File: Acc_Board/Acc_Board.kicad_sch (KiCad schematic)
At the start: 43 parts, among them J1 1053091202, J11 1053091202, J12 776087-1, J2 1053091202, J3 1053091202, J4 1053091202, J5 1053091202, J6 1053091202, J9 1053091202, K1 Relay_SPST-NO, U1 ISO1050DUB, U13 R-78B5.0-2.0, U2 NUCLEO-L432KC, U4 PQDE6W-Q110-S5-H-D

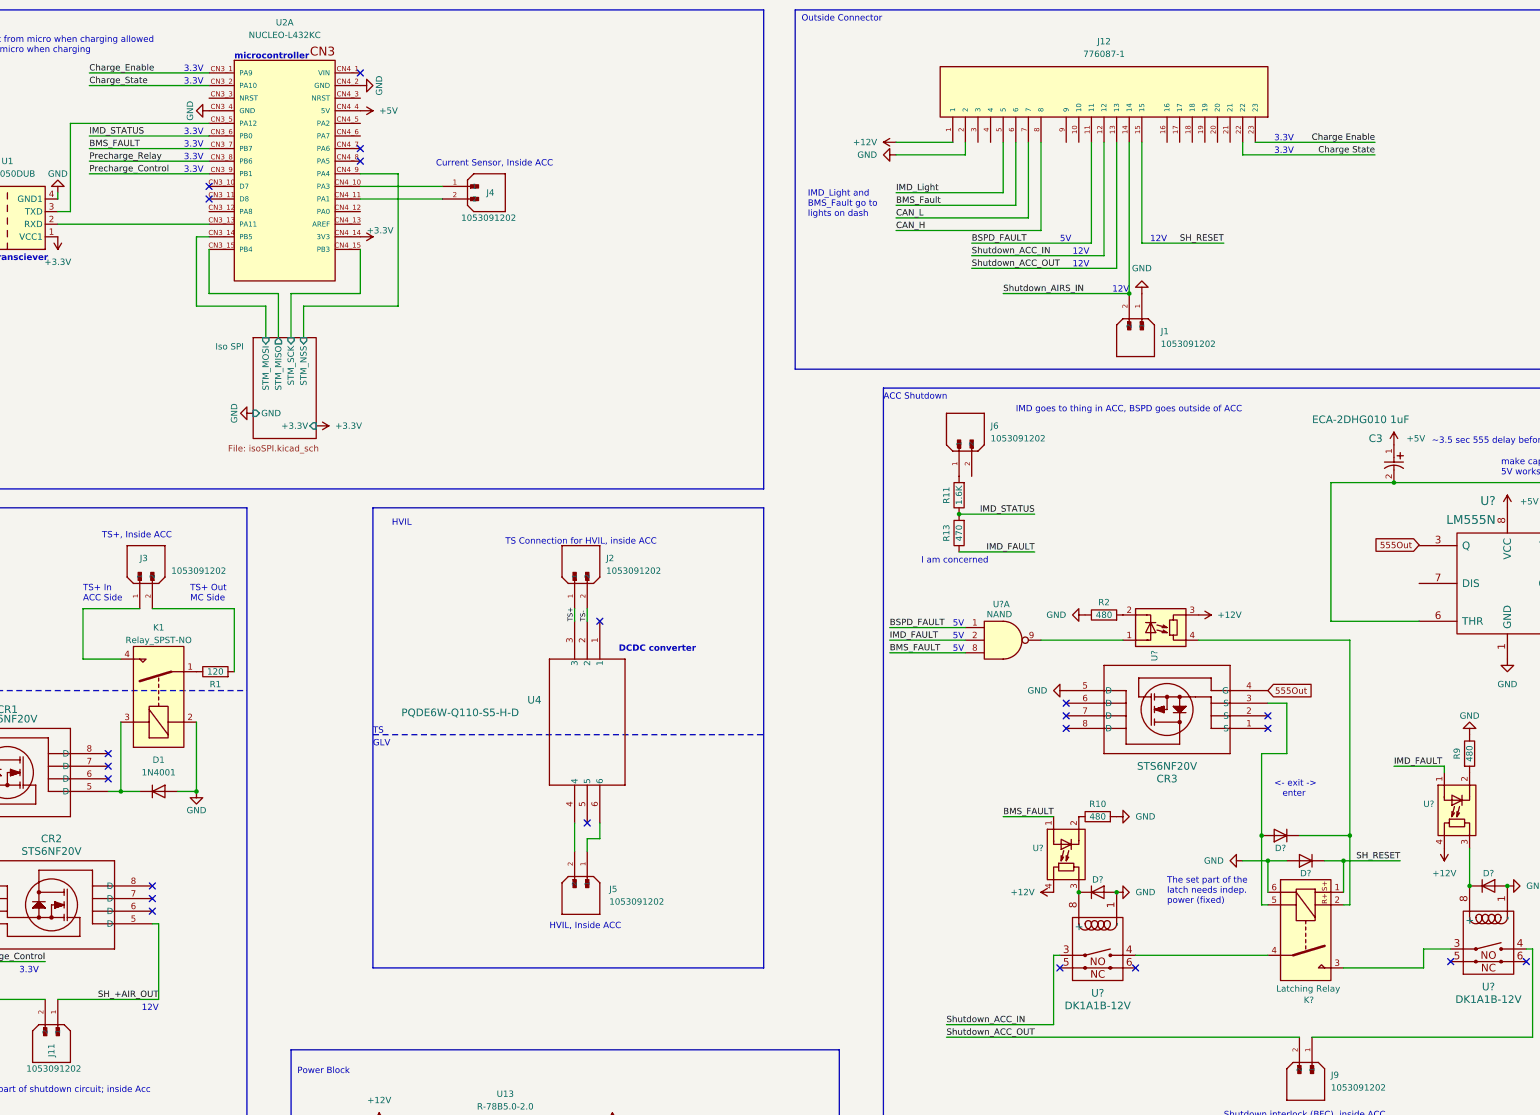
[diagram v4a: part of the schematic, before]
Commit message: Minor trace changes to acc board
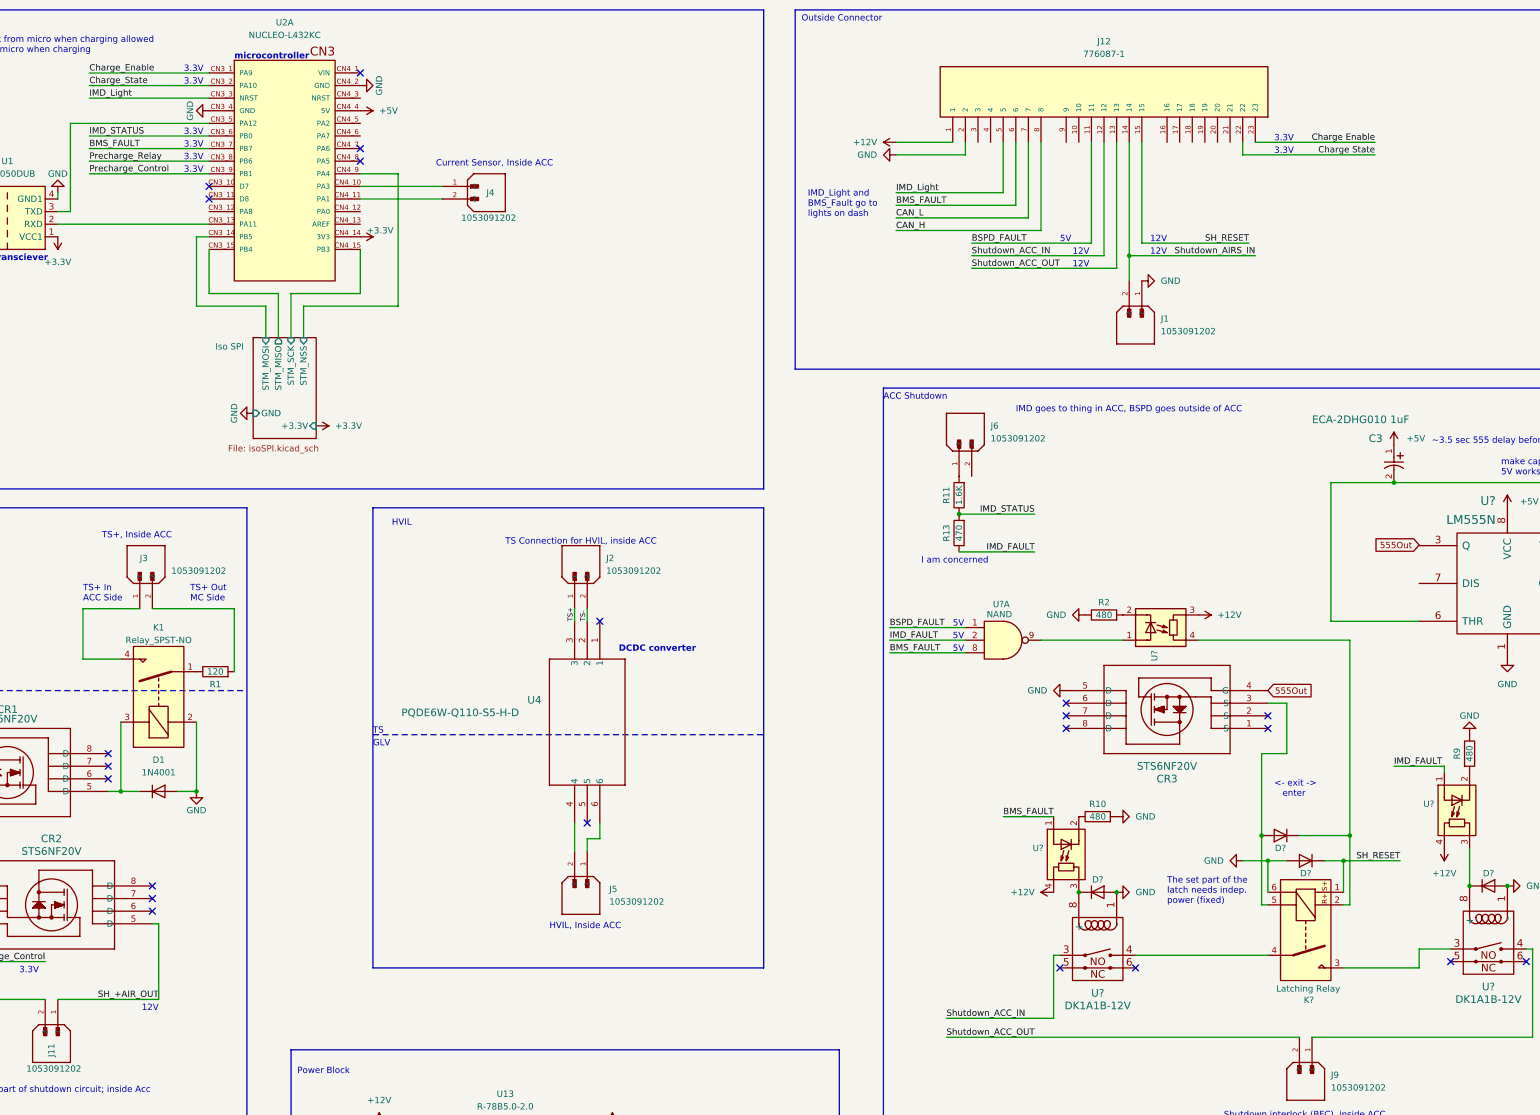
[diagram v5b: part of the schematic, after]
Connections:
- net BMS_Fault is gone; now on net BMS_FAULT: J12.6
- net IMD_Light: now also U2.CN3_3 (NRST)
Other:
- moved on the sheet: J1
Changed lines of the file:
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@@
   (junction (at 156.21 247.65) (diameter 0) (color 0 0 0 0)
   )
+  (junction (at 281.94 64.77) (diameter 0) (color 0 0 0 0)
+  )
   (junction (at 308.61 181.61) (diameter 0) (color 0 0 0 0)
   )
@@
   )
   (junction (at 130.81 240.03) (diameter 0) (color 0 0 0 0)
-  )
-  (junction (at 281.94 72.39) (diameter 0) (color 0 0 0 0)
   )
   (junction (at 247.65 116.84) (diameter 0) (color 0 0 0 0)
@@
   (no_connect (at 175.26 138.43))
   (wire (pts (xy 363.22 204.47) (xy 361.95 204.47))
-    (stroke (width 0) (type default))
+    (stroke (width 1) (type default))
   )
   (wire (pts (xy 345.44 167.64) (xy 345.44 168.91))
@@
   )
   (wire (pts (xy 283.21 205.74) (xy 309.88 205.74))
-    (stroke (width 0) (type default))
+    (stroke (width 1) (type default))
   )
   (wire (pts (xy 234.95 59.69) (xy 264.16 59.69))
@@
     (stroke (width 0) (type default))
   )
-  (wire (pts (xy 256.54 72.39) (xy 281.94 72.39))
-    (stroke (width 0) (type default))
-  )
   (wire (pts (xy 234.95 44.45) (xy 248.92 44.45))
     (stroke (width 0) (type default))
@@
     (stroke (width 0) (type default))
   )
-  (wire (pts (xy 341.249 204.47) (xy 346.71 204.47))
-    (stroke (width 0) (type default))
+  (wire (pts (xy 340.36 204.47) (xy 346.71 204.47))
+    (stroke (width 1) (type default))
   )
   (wire (pts (xy 63.5 207.01) (xy 44.45 207.01))
@@
     (stroke (width 0) (type default))
   )
+  (wire (pts (xy 325.12 208.28) (xy 340.36 208.28))
+    (stroke (width 1) (type default))
+  )
   (wire (pts (xy 383.54 123.19) (xy 387.35 123.19))
     (stroke (width 0) (type default))
@@
     (stroke (width 0) (type default))
   )
-  (wire (pts (xy 341.249 204.47) (xy 341.249 208.28))
-    (stroke (width 0) (type default))
+  (wire (pts (xy 340.36 204.47) (xy 340.36 208.28))
+    (stroke (width 1) (type default))
   )
   (wire (pts (xy 264.16 41.91) (xy 264.16 59.69))
@@
     (stroke (width 0) (type default))
   )
-  (wire (pts (xy 245.11 219.71) (xy 266.7 219.71))
-    (stroke (width 0) (type default))
+  (wire (pts (xy 245.11 218.44) (xy 266.7 218.44))
+    (stroke (width 1) (type default))
   )
   (wire (pts (xy 304.8 41.91) (xy 304.8 44.45))
@@
     (stroke (width 0) (type default))
   )
+  (wire (pts (xy 72.39 33.02) (xy 96.52 33.02))
+    (stroke (width 0) (type default))
+  )
   (wire (pts (xy 66.04 214.63) (xy 86.36 214.63))
     (stroke (width 0) (type default))
@@
     (stroke (width 0) (type default))
   )
-  (wire (pts (xy 341.249 208.28) (xy 325.12 208.28))
-    (stroke (width 0) (type default))
-  )
   (wire (pts (xy 309.88 186.69) (xy 309.88 193.04))
     (stroke (width 0) (type default))
@@
     (stroke (width 0) (type default))
   )
-  (wire (pts (xy 266.7 205.74) (xy 266.7 219.71))
-    (stroke (width 0) (type default))
+  (wire (pts (xy 266.7 205.74) (xy 266.7 218.44))
+    (stroke (width 1) (type default))
   )
   (wire (pts (xy 68.58 55.88) (xy 68.58 38.1))
@@
   )
   (wire (pts (xy 318.77 222.25) (xy 363.22 222.25))
-    (stroke (width 0) (type default))
+    (stroke (width 1) (type default))
   )
   (wire (pts (xy 322.58 138.43) (xy 340.36 138.43))
@@
   )
   (wire (pts (xy 267.97 205.74) (xy 266.7 205.74))
-    (stroke (width 0) (type default))
+    (stroke (width 1) (type default))
   )
   (wire (pts (xy 38.1 60.96) (xy 40.64 60.96))
@@
     (stroke (width 0) (type default))
   )
+  (wire (pts (xy 307.34 64.77) (xy 281.94 64.77))
+    (stroke (width 0) (type default))
+  )
   (wire (pts (xy 308.61 165.1) (xy 313.69 165.1))
     (stroke (width 0) (type default))
@@
     (stroke (width 0) (type default))
   )
-  (wire (pts (xy 300.99 62.23) (xy 284.48 62.23))
+  (wire (pts (xy 306.07 62.23) (xy 284.48 62.23))
     (stroke (width 0) (type default))
   )
@@
   )
   (wire (pts (xy 245.11 222.25) (xy 316.23 222.25))
-    (stroke (width 0) (type default))
-  )
-  (wire (pts (xy 281.94 41.91) (xy 281.94 72.39))
+    (stroke (width 1) (type default))
+  )
+  (wire (pts (xy 281.94 41.91) (xy 281.94 64.77))
     (stroke (width 0) (type default))
   )
@@
   )
   (wire (pts (xy 363.22 204.47) (xy 363.22 222.25))
-    (stroke (width 0) (type default))
+    (stroke (width 1) (type default))
   )
   (wire (pts (xy 38.1 53.34) (xy 40.64 53.34))
@@
   )
   (wire (pts (xy 170.18 138.43) (xy 170.18 135.89))
+    (stroke (width 0) (type default))
+  )
+  (wire (pts (xy 281.94 64.77) (xy 281.94 69.85))
     (stroke (width 0) (type default))
   )
@@
     (effects (font (size 1.27 1.27)) (justify left bottom))
   )
-  (text "12V" (at 281.94 72.39 0)
+  (text "12V" (at 289.56 64.77 0)
     (effects (font (size 1.27 1.27)) (justify right bottom))
   )
@@
     (effects (font (size 1.27 1.27)) (justify left bottom))
   )
+  (label "IMD_Light" (at 72.39 33.02 0) (fields_autoplaced)
+    (effects (font (size 1.27 1.27)) (justify left bottom))
+  )
   (label "Shutdown_ACC_OUT" (at 250.19 67.31 0) (fields_autoplaced)
     (effects (font (size 1.27 1.27)) (justify left bottom))
   )
-  (label "BMS_Fault" (at 234.95 54.61 0) (fields_autoplaced)
+  (label "BMS_FAULT" (at 234.95 54.61 0) (fields_autoplaced)
     (effects (font (size 1.27 1.27)) (justify left bottom))
   )
@@
     (effects (font (size 1.27 1.27)) (justify left bottom))
   )
-  (label "SH_RESET" (at 300.99 62.23 180) (fields_autoplaced)
+  (label "SH_RESET" (at 306.07 62.23 180) (fields_autoplaced)
     (effects (font (size 1.27 1.27)) (justify right bottom))
   )
@@
     (effects (font (size 1.27 1.27)) (justify right bottom))
   )
-  (label "Shutdown_AIRS_IN" (at 256.54 72.39 0) (fields_autoplaced)
-    (effects (font (size 1.27 1.27)) (justify left bottom))
-  )
-  (label "Shutdown_ACC_IN" (at 245.11 219.71 0) (fields_autoplaced)
+  (label "Shutdown_AIRS_IN" (at 307.34 64.77 180) (fields_autoplaced)
+    (effects (font (size 1.27 1.27)) (justify right bottom))
+  )
+  (label "Shutdown_ACC_IN" (at 245.11 218.44 0) (fields_autoplaced)
     (effects (font (size 1.27 1.27)) (justify left bottom))
   )
@@
     )
   )
-  (symbol (lib_id "power:GND") (at 284.48 72.39 180) (unit 1)
-    (in_bom yes) (on_board yes) (dnp no) (fields_autoplaced)
-    (property "Reference" "#PWR041" (at 284.48 66.04 0)
-      (effects (font (size 1.27 1.27)) hide)
-    )
-    (property "Value" "GND" (at 284.48 67.31 0)
-      (effects (font (size 1.27 1.27)))
-    )
-    (property "Footprint" "" (at 284.48 72.39 0)
-      (effects (font (size 1.27 1.27)) hide)
-    )
-    (property "Datasheet" "" (at 284.48 72.39 0)
+  (symbol (lib_id "power:GND") (at 284.48 69.85 90) (unit 1)
+    (in_bom yes) (on_board yes) (dnp no) (fields_autoplaced)
+    (property "Reference" "#PWR041" (at 290.83 69.85 0)
+      (effects (font (size 1.27 1.27)) hide)
+    )
+    (property "Value" "GND" (at 288.29 69.85 90)
+      (effects (font (size 1.27 1.27)) (justify right))
+    )
+    (property "Footprint" "" (at 284.48 69.85 0)
+      (effects (font (size 1.27 1.27)) hide)
+    )
+    (property "Datasheet" "" (at 284.48 69.85 0)
       (effects (font (size 1.27 1.27)) hide)
     )
@@
     )
   )
-  (symbol (lib_id "molex_1053091202:1053091202") (at 284.48 77.47 270) (unit 1)
-    (in_bom yes) (on_board yes) (dnp no) (fields_autoplaced)
-    (property "Reference" "J1" (at 288.29 80.01 90)
-      (effects (font (size 1.27 1.27)) (justify left))
-    )
-    (property "Value" "1053091202" (at 288.29 82.55 90)
-      (effects (font (size 1.27 1.27)) (justify left))
-    )
-    (property "Footprint" "1FS_2_Global_Footprint_Library:MOLEX_1053091202" (at 284.48 77.47 0)
-      (effects (font (size 1.27 1.27)) (justify bottom) hide)
-    )
-    (property "Datasheet" "" (at 284.48 77.47 0)
-      (effects (font (size 1.27 1.27)) hide)
-    )
-    (property "PARTREV" "H" (at 284.48 77.47 0)
-      (effects (font (size 1.27 1.27)) (justify bottom) hide)
-    )
-    (property "STANDARD" "Manufacturer Recommendations" (at 284.48 77.47 0)
-      (effects (font (size 1.27 1.27)) (justify bottom) hide)
-    )
-    (property "MAXIMUM_PACKAGE_HEIGHT" "10.51 mm" (at 284.48 77.47 0)
-      (effects (font (size 1.27 1.27)) (justify bottom) hide)
-    )
-    (property "MANUFACTURER" "Molex" (at 284.48 77.47 0)
-      (effects (font (size 1.27 1.27)) (justify bottom) hide)
-    )
+  (symbol (lib_id "molex_1053091202:1053091202") (at 284.48 74.93 270) (unit 1)
+    (in_bom yes) (on_board yes) (dnp no) (fields_autoplaced)
+    (property "Reference" "J1" (at 288.29 77.47 90)
+      (effects (font (size 1.27 1.27)) (justify left))
+    )
+    (property "Value" "1053091202" (at 288.29 80.01 90)
+      (effects (font (size 1.27 1.27)) (justify left))
+    )
+    (property "Footprint" "1FS_2_Global_Footprint_Library:MOLEX_1053091202" (at 284.48 74.93 0)
+      (effects (font (size 1.27 1.27)) (justify bottom) hide)
+    )
+    (property "Datasheet" "" (at 284.48 74.93 0)
+      (effects (font (size 1.27 1.27)) hide)
+    )
+    (property "PARTREV" "H" (at 284.48 74.93 0)
+      (effects (font (size 1.27 1.27)) (justify bottom) hide)
+    )
+    (property "STANDARD" "Manufacturer Recommendations" (at 284.48 74.93 0)
+      (effects (font (size 1.27 1.27)) (justify bottom) hide)
+    )
+    (property "MAXIMUM_PACKAGE_HEIGHT" "10.51 mm" (at 284.48 74.93 0)
+      (effects (font (size 1.27 1.27)) (justify bottom) hide)
+    )
+    (property "MANUFACTURER" "Molex" (at 284.48 74.93 0)
+      (effects (font (size 1.27 1.27)) (justify bottom) hide)
+    )
